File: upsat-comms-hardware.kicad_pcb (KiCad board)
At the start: 4 copper layers, 92.5 x 92.5 mm, 314 parts, among them U1 TXCO_TG_5021CG, U10 CC1120, U12 ADT7420, U14 OPA320, U16 RF5110G, U18 FA_128_, U2 TPS79930, U3 FA_128_, U4 CC1120, U5 STM32F407VG, U6 TXCO_TG_5021CG, U8 TPS79930, Y1 Crystal, Y2 Crystal

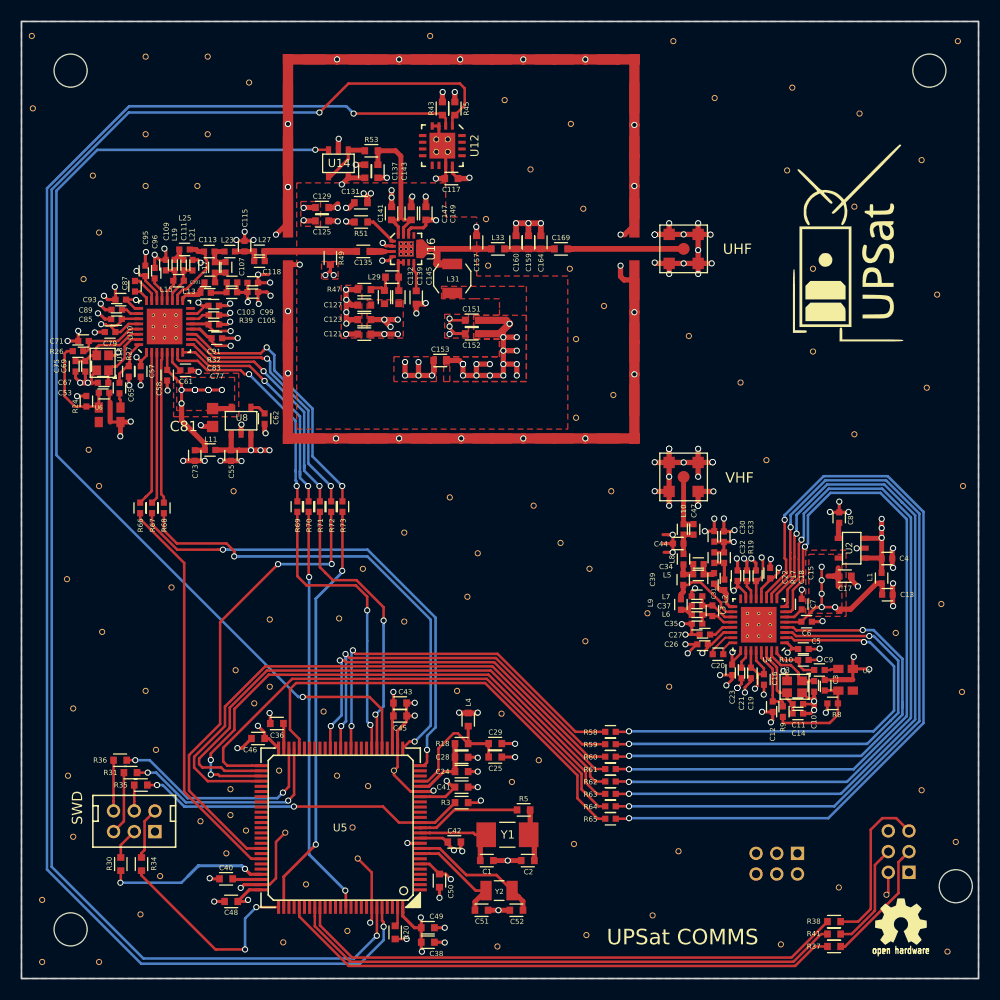
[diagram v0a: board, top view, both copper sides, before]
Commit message: New footprint for RF5110G.
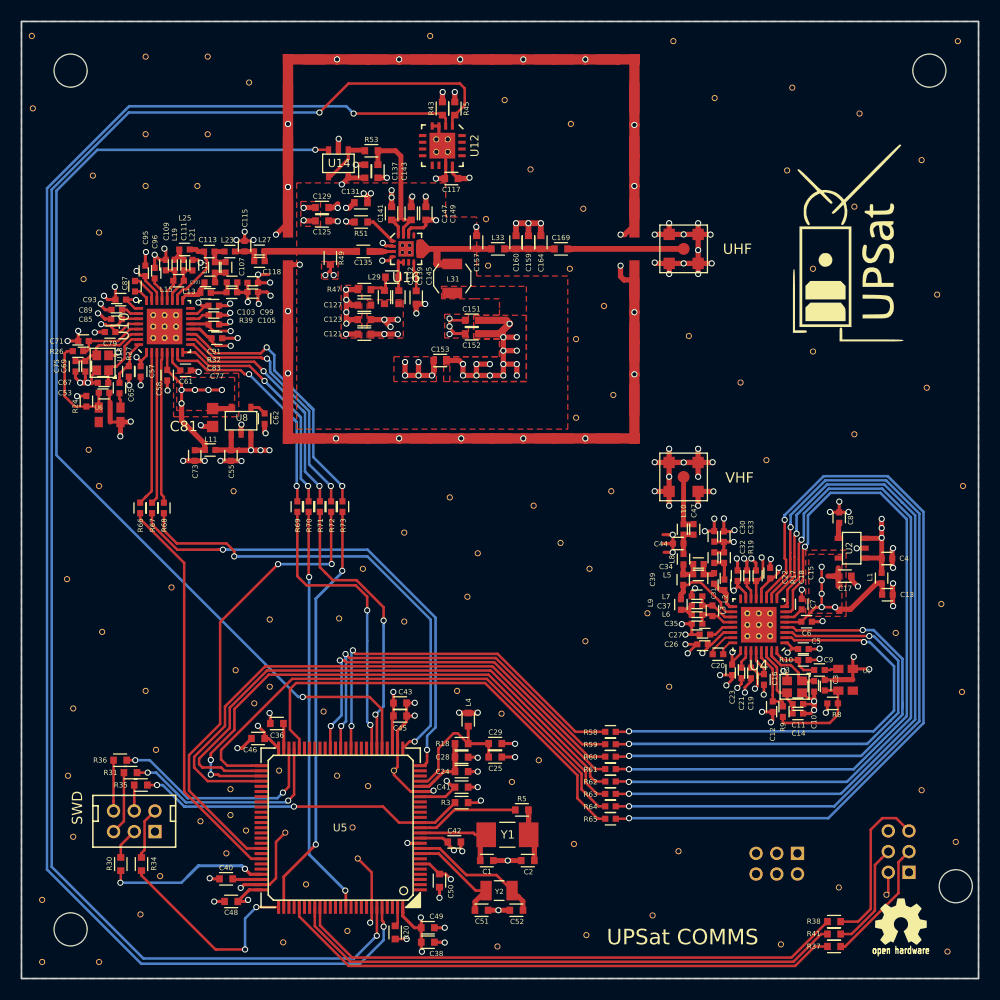
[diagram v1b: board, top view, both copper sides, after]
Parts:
- moved R5 0.17 mm to (150.2, 130.8)
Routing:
- net Net-(C135-Pad1): track 3.47 -> 2.83 mm
- net Net-(R73-Pad2): track 26.3 -> 26.9 mm
- net GND: track 369.4 -> 369.1 mm, vias 184 -> 179
- net VDD: vias 30 -> 28
- net +3V3: vias 47 -> 46

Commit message: Routing changes and package fixes.
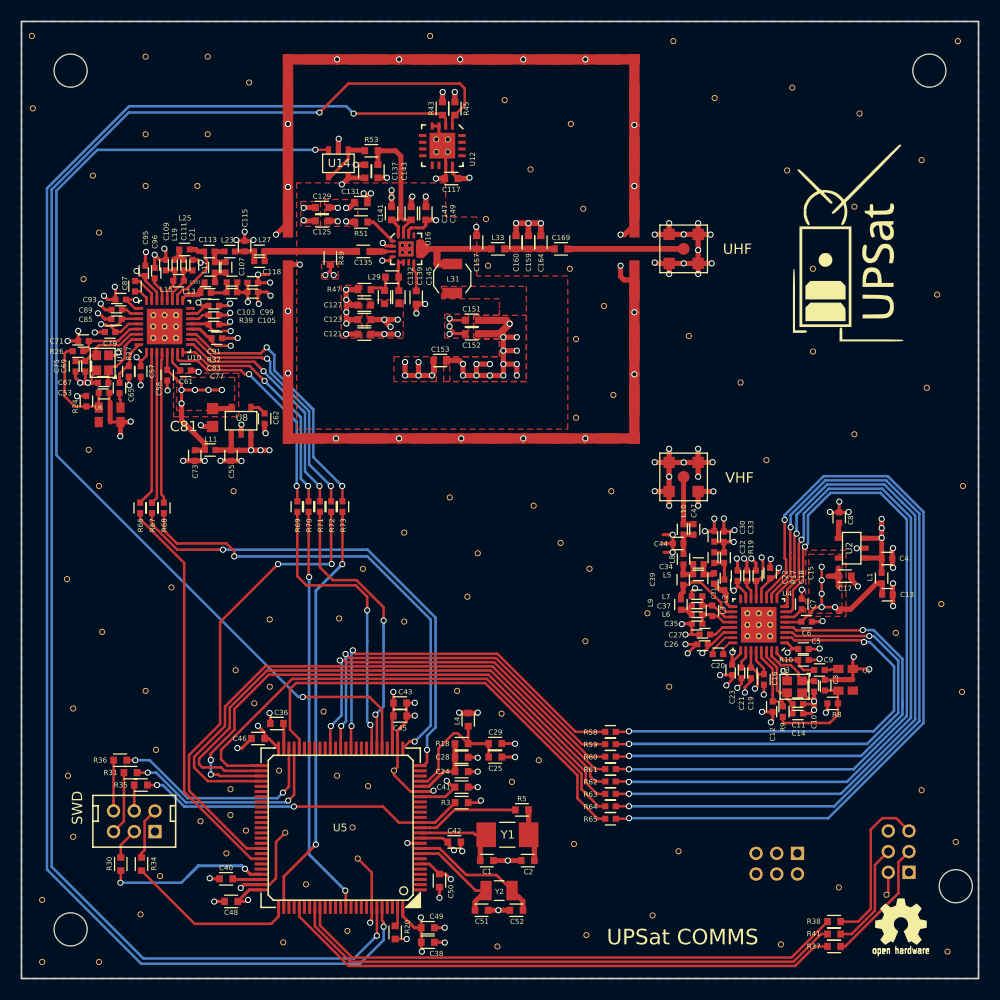
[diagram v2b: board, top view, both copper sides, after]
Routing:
- net /SWCLK: track 20.2 -> 16.6 mm, vias 2 -> 0
- net +3V3: track 101.8 -> 101.2 mm
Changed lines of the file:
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@@
     (thickness 1.55)
     (drawings 10345)
-    (tracks 1947)
+    (tracks 1937)
     (zones 0)
     (modules 314)
@@
   (layers
     (0 F.Cu signal)
-    (1 In1.Cu signal hide)
+    (1 In1.Cu signal)
     (2 In2.Cu signal)
     (31 B.Cu signal)
@@
     (35 F.Paste user hide)
     (36 B.SilkS user hide)
-    (37 F.SilkS user hide)
+    (37 F.SilkS user)
     (38 B.Mask user hide)
     (39 F.Mask user hide)
@@
     (solder_mask_margin 0.1)
     (attr smd)
-    (fp_text reference U12 (at 0 -3.125 270) (layer F.SilkS)
-      (effects (font (size 0.8 0.8) (thickness 0.1)))
+    (fp_text reference U12 (at 1.3 -2.925 270) (layer F.SilkS)
+      (effects (font (size 0.5 0.5) (thickness 0.1)))
     )
     (fp_text value ADT7420 (at 0 3.36 270) (layer F.Fab)
@@
   (module libs:0402_cc (layer F.Cu)
     (at 166.484692 106.055988 270)
-    (fp_text reference L8 (at 0.51 1.11 270) (layer F.SilkS)
+    (fp_text reference L8 (at 0.51 1.084692 270) (layer F.SilkS)
       (effects (font (size 0.5 0.5) (thickness 0.1)))
     )
@@
   (module libs:0603murata2 (layer F.Cu)
     (at 127.82 122.45 180)
-    (fp_text reference C36 (at 0.62 -1.15 180) (layer F.SilkS)
+    (fp_text reference C36 (at 0.22 1.05 180) (layer F.SilkS)
       (effects (font (size 0.5 0.5) (thickness 0.1)))
     )
@@
   (module libs:0603murata2 (layer F.Cu)
     (at 126 123.9 180)
-    (fp_text reference C46 (at 1.4 -1.1 180) (layer F.SilkS)
+    (fp_text reference C46 (at 2.4 0 180) (layer F.SilkS)
       (effects (font (size 0.5 0.5) (thickness 0.1)))
     )
@@
   (module libs:0603murata2 (layer F.Cu)
     (at 145.68 122.71 90)
-    (fp_text reference L4 (at 2.31 0.02 90) (layer F.SilkS)
+    (fp_text reference L4 (at 0.51 -1.08 90) (layer F.SilkS)
       (effects (font (size 0.5 0.5) (thickness 0.1)))
     )
@@
   (module libs:0603murata2 (layer F.Cu)
     (at 138.62 142.01 270)
-    (fp_text reference R20 (at 0.64 -1.07 270) (layer F.SilkS)
+    (fp_text reference R20 (at 0.09 -1.18 270) (layer F.SilkS)
       (effects (font (size 0.5 0.5) (thickness 0.1)))
     )
@@
     (solder_mask_margin 0.07)
     (attr smd)
-    (fp_text reference U10 (at 0 -3.925 90) (layer F.SilkS)
-      (effects (font (size 1 1) (thickness 0.15)))
+    (fp_text reference U10 (at -3.018672 2.86524 180) (layer F.SilkS)
+      (effects (font (size 0.5 0.5) (thickness 0.1)))
     )
     (fp_text value CC1120 (at 0 3.925 90) (layer F.Fab)
@@
     (solder_mask_margin 0.07)
     (attr smd)
-    (fp_text reference U4 (at 0 -3.925 180) (layer F.SilkS)
-      (effects (font (size 1 1) (thickness 0.15)))
+    (fp_text reference U4 (at -2.740308 3.005988 180) (layer F.SilkS)
+      (effects (font (size 0.5 0.5) (thickness 0.1)))
     )
     (fp_text value CC1120 (at 0 3.925 180) (layer F.Fab)
@@
     (at 139.67238 76.581328)
     (solder_mask_margin 0.05)
-    (fp_text reference U16 (at 0 2.75) (layer F.SilkS)
-      (effects (font (size 1 1) (thickness 0.15)))
+    (fp_text reference U16 (at 2.12762 -0.981328 90) (layer F.SilkS)
+      (effects (font (size 0.5 0.5) (thickness 0.1)))
     )
     (fp_text value RF5110G (at 0 -3) (layer F.Fab)
@@
   (via (at 133.07238 72.615664) (size 0.6) (drill 0.4) (layers F.Cu B.Cu) (net 5))
   (segment (start 132.18476 72.581328) (end 132.706716 72.581328) (width 0.508) (layer F.Cu) (net 5))
-  (segment (start 132.706716 72.581328) (end 133.07238 72.215664) (width 0.508) (layer F.Cu) (net 5))
   (via (at 133.87238 84.815664) (size 0.6) (drill 0.4) (layers F.Cu B.Cu) (net 5))
   (segment (start 135.00238 80.515664) (end 133.87238 80.515664) (width 0.508) (layer F.Cu) (net 5))
@@
   (segment (start 119.656716 83.331328) (end 120.006716 82.981328) (width 0.25) (layer F.Cu) (net 77))
   (segment (start 120.006716 82.981328) (end 120.58476 82.981328) (width 0.25) (layer F.Cu) (net 77))
-  (segment (start 114.1 137.095) (end 114.1 136.67) (width 0.25) (layer F.Cu) (net 78))
-  (segment (start 121.248908 144.29) (end 114.1 137.141092) (width 0.25) (layer F.Cu) (net 78))
-  (segment (start 121.35 144.29) (end 121.248908 144.29) (width 0.25) (layer F.Cu) (net 78))
-  (segment (start 114.1 137.141092) (end 114.1 137.095) (width 0.25) (layer F.Cu) (net 78))
-  (segment (start 124.03 144.29) (end 124.11 144.21) (width 0.25) (layer F.Cu) (net 78))
-  (segment (start 121.35 144.29) (end 124.03 144.29) (width 0.25) (layer F.Cu) (net 78))
-  (segment (start 124.11 144.21) (end 124.11 144.29) (width 0.25) (layer F.Cu) (net 78))
-  (segment (start 124.11 141.29) (end 124.11 143.865736) (width 0.25) (layer B.Cu) (net 78))
-  (segment (start 125.2 140.2) (end 124.11 141.29) (width 0.25) (layer B.Cu) (net 78))
-  (segment (start 124.11 143.865736) (end 124.11 144.29) (width 0.25) (layer B.Cu) (net 78))
-  (via (at 124.11 144.29) (size 0.6) (drill 0.4) (layers F.Cu B.Cu) (net 78))
-  (segment (start 125.2 140.2) (end 127.34964 140.2) (width 0.25) (layer F.Cu) (net 78))
+  (segment (start 119.238905 141.808905) (end 126.644495 141.808905) (width 0.25) (layer F.Cu) (net 78))
+  (segment (start 127.3514 140.20176) (end 127.3514 141.102) (width 0.25) (layer F.Cu) (net 78))
+  (segment (start 127.3514 141.102) (end 126.644495 141.808905) (width 0.25) (layer F.Cu) (net 78))
+  (segment (start 114.1 136.67) (end 119.238905 141.808905) (width 0.25) (layer F.Cu) (net 78))
   (segment (start 127.34964 140.2) (end 127.3514 140.20176) (width 0.25) (layer F.Cu) (net 78))
-  (via (at 125.2 140.2) (size 0.6) (drill 0.4) (layers F.Cu B.Cu) (net 78))
   (segment (start 113.5 126) (end 114.892247 126) (width 0.25) (layer B.Cu) (net 79))
   (segment (start 114.892247 126) (end 118.562914 129.670667) (width 0.25) (layer B.Cu) (net 79))
@@
   (segment (start 113.97238 102.125664) (end 113.97238 102.680664) (width 0.25) (layer F.Cu) (net 101))
   (segment (start 113.97238 102.125664) (end 113.97238 102.135664) (width 0.25) (layer F.Cu) (net 101))
-  (segment (start 133.52238 102) (end 133.52238 107.671609) (width 0.25) (layer F.Cu) (net 102))
-  (segment (start 133.52238 107.671609) (end 133.499989 107.694) (width 0.25) (layer F.Cu) (net 102))
-  (segment (start 133.499989 107.833849) (end 133.499989 107.694) (width 0.27) (layer B.Cu) (net 102))
-  (segment (start 130.949027 134.150973) (end 130.949027 110.384811) (width 0.27) (layer B.Cu) (net 102))
-  (segment (start 130.949027 110.384811) (end 133.499989 107.833849) (width 0.27) (layer B.Cu) (net 102))
-  (via (at 133.499989 107.694) (size 0.6) (drill 0.4) (layers F.Cu B.Cu) (net 102))
+  (segment (start 133.212011 107.35253) (end 133.51201 107.052531) (width 0.27) (layer B.Cu) (net 102))
+  (segment (start 130.949027 109.615514) (end 133.212011 107.35253) (width 0.27) (layer B.Cu) (net 102))
+  (segment (start 130.949027 134.150973) (end 130.949027 109.615514) (width 0.27) (layer B.Cu) (net 102))
+  (segment (start 133.52238 107.042161) (end 133.51201 107.052531) (width 0.25) (layer F.Cu) (net 102))
+  (segment (start 133.52238 102) (end 133.52238 107.042161) (width 0.25) (layer F.Cu) (net 102))
+  (via (at 133.51201 107.052531) (size 0.6) (drill 0.4) (layers F.Cu B.Cu) (net 102))
   (via (at 130.949027 134.150973) (size 0.6) (drill 0.4) (layers F.Cu B.Cu) (net 102))
   (segment (start 127.85178 137.24822) (end 130.649028 134.450972) (width 0.27) (layer F.Cu) (net 102))
@@
       )
     )
+  )
+  (zone (net 5) (net_name +3V3) (layer F.Cu) (hatch edge 0.508)
+    (connect_pads yes (clearance 0.25))
+    (min_thickness 0.25)
+    (fill yes (arc_segments 32) (thermal_gap 0.508) (thermal_bridge_width 0.508))
+    (polygon
+      (pts
+        (xy 131.8 74.4) (xy 135 74.4) (xy 135 71.8) (xy 131.8 71.8)
+      )
+    )

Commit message: Fix silkscreen specs.
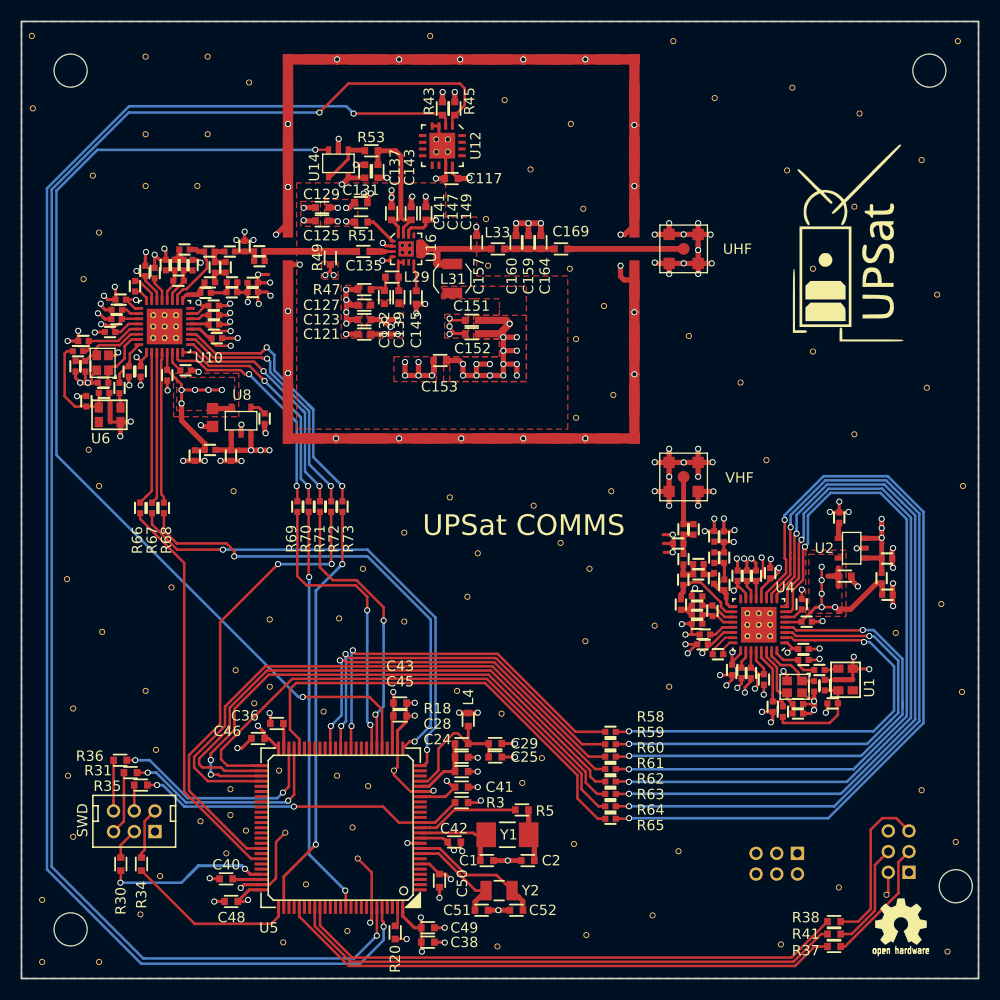
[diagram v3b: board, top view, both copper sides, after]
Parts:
- R3: value 220 -> 10K
- moved U1 2.50 mm to (181.4, 119.2), turned to 90 degrees
- moved REF** 1.39 mm to (163.7, 113.0)
- moved REF** 1.00 mm to (150.9, 128.2)
- moved REF** 0.36 mm to (152.8, 125.8)

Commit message: Exchange SOT23-5 footprint.
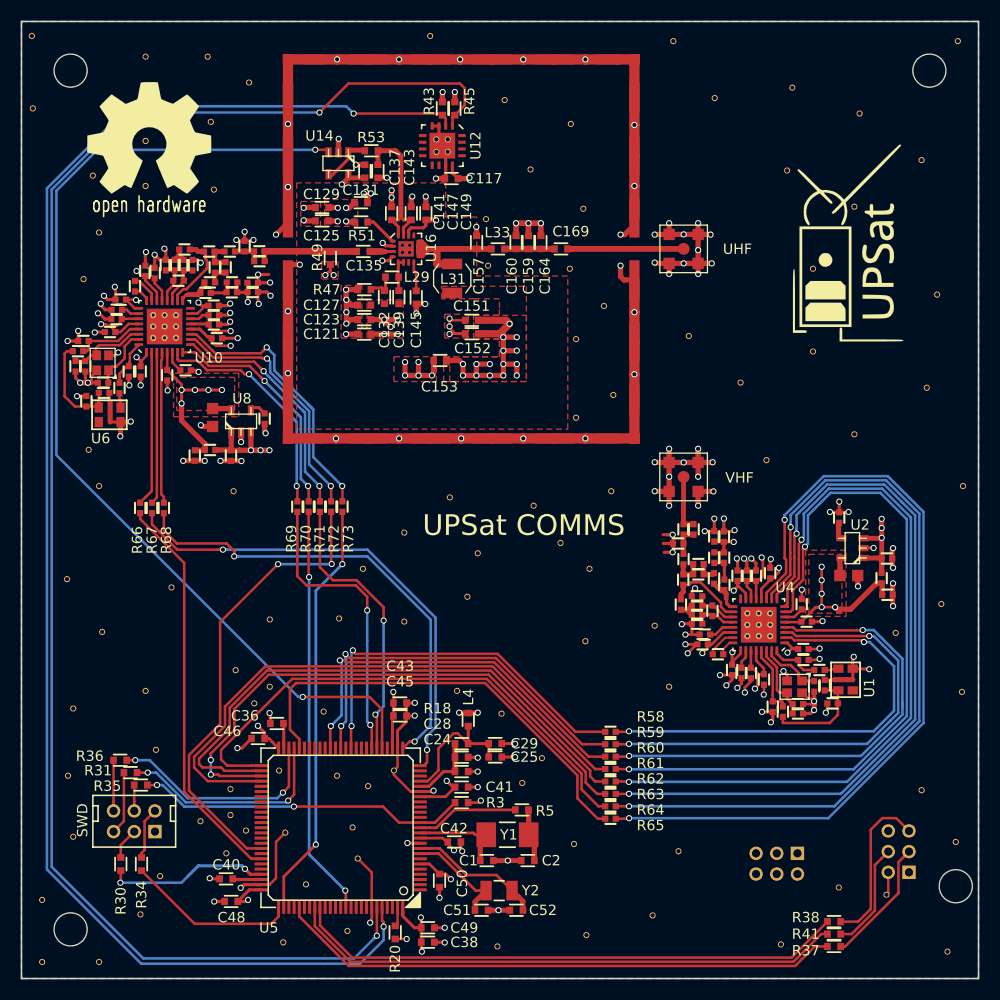
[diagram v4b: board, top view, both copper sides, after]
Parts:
- removed the G*** at (187.5, 141.6)
- added G***: LOGO, w_logo:Logo_silk_OSHW_12x13mm, F.Cu at (114.8, 65.8)
- C17: footprint libs:0603murata2 -> libs:CC1120DecCAP
- U14, U2, U8: footprint libs:SOT23-5 -> w_smd_trans:sot23-5
- moved C17 1.86 mm to (183.3, 108.2), turned to 90 degrees
- moved REF** 1.64 mm to (121.1, 70.8)
- moved REF** 1.24 mm to (120.8, 64.3)
- moved REF** 0.65 mm to (114.5, 66.2)
- moved U2 0.07 mm to (182.8, 105.5)
- moved U8 0.06 mm to (123.7, 93.2)
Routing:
- net VDD: track 105.9 -> 104.8 mm
